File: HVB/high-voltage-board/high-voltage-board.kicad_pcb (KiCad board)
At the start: 2 copper layers, 181.6 x 106 mm, 73 parts, among them J1 Conn_01x23, J10 Conn_01x05, J11 HV-, J2 HECS, J3 HV+, J4 HV-, J5 HV+, J6 HV-, J7 Conn_01x02, J8 HV+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

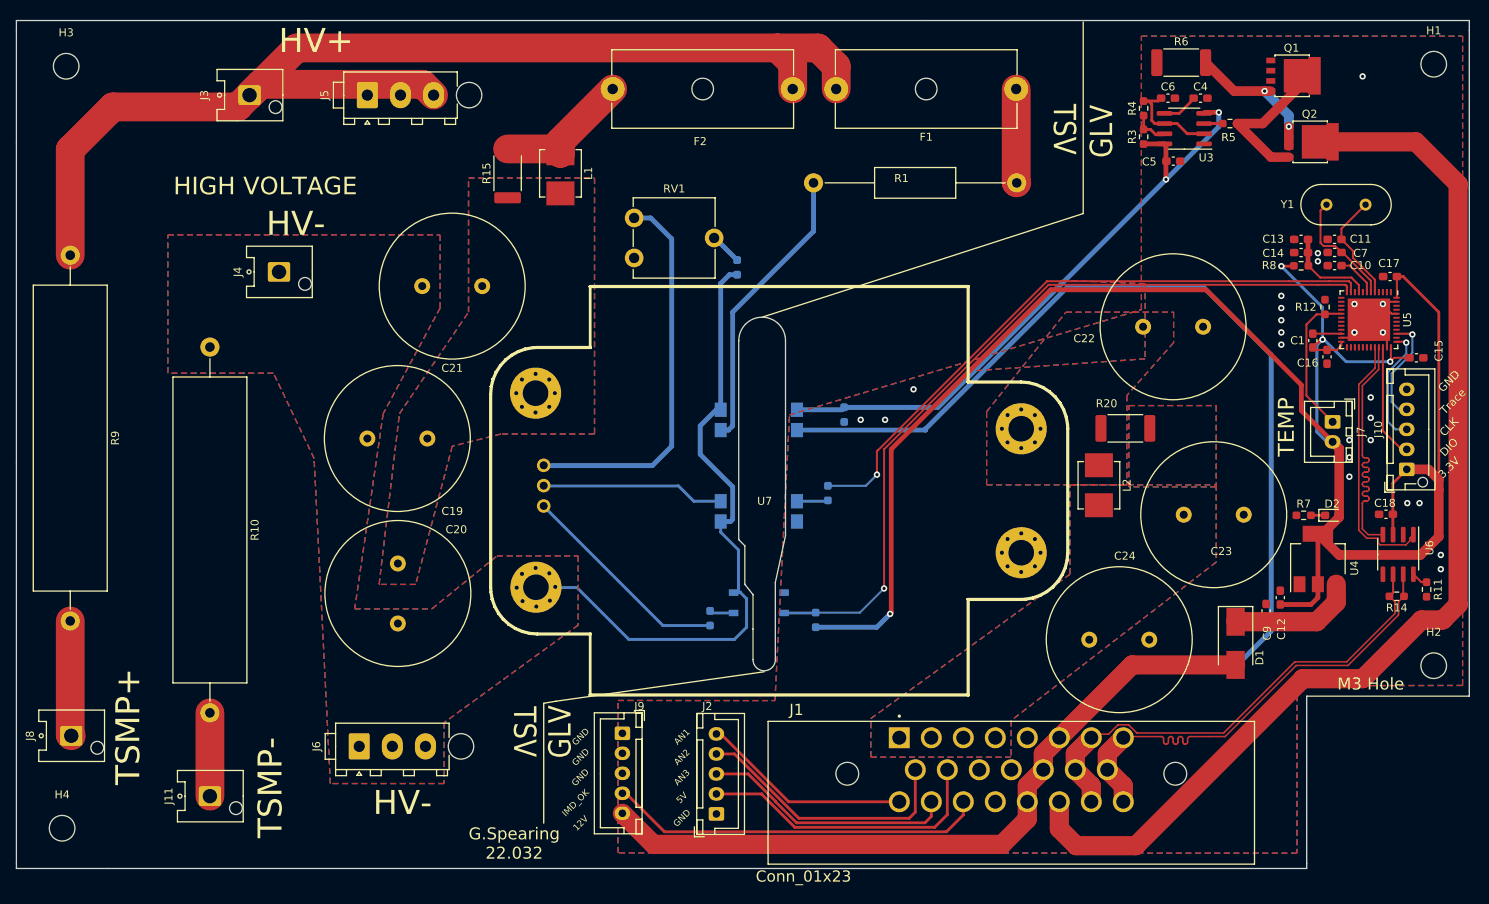
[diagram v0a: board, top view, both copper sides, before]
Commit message: Major Review and Part Update
updating footprints, component values, layouts
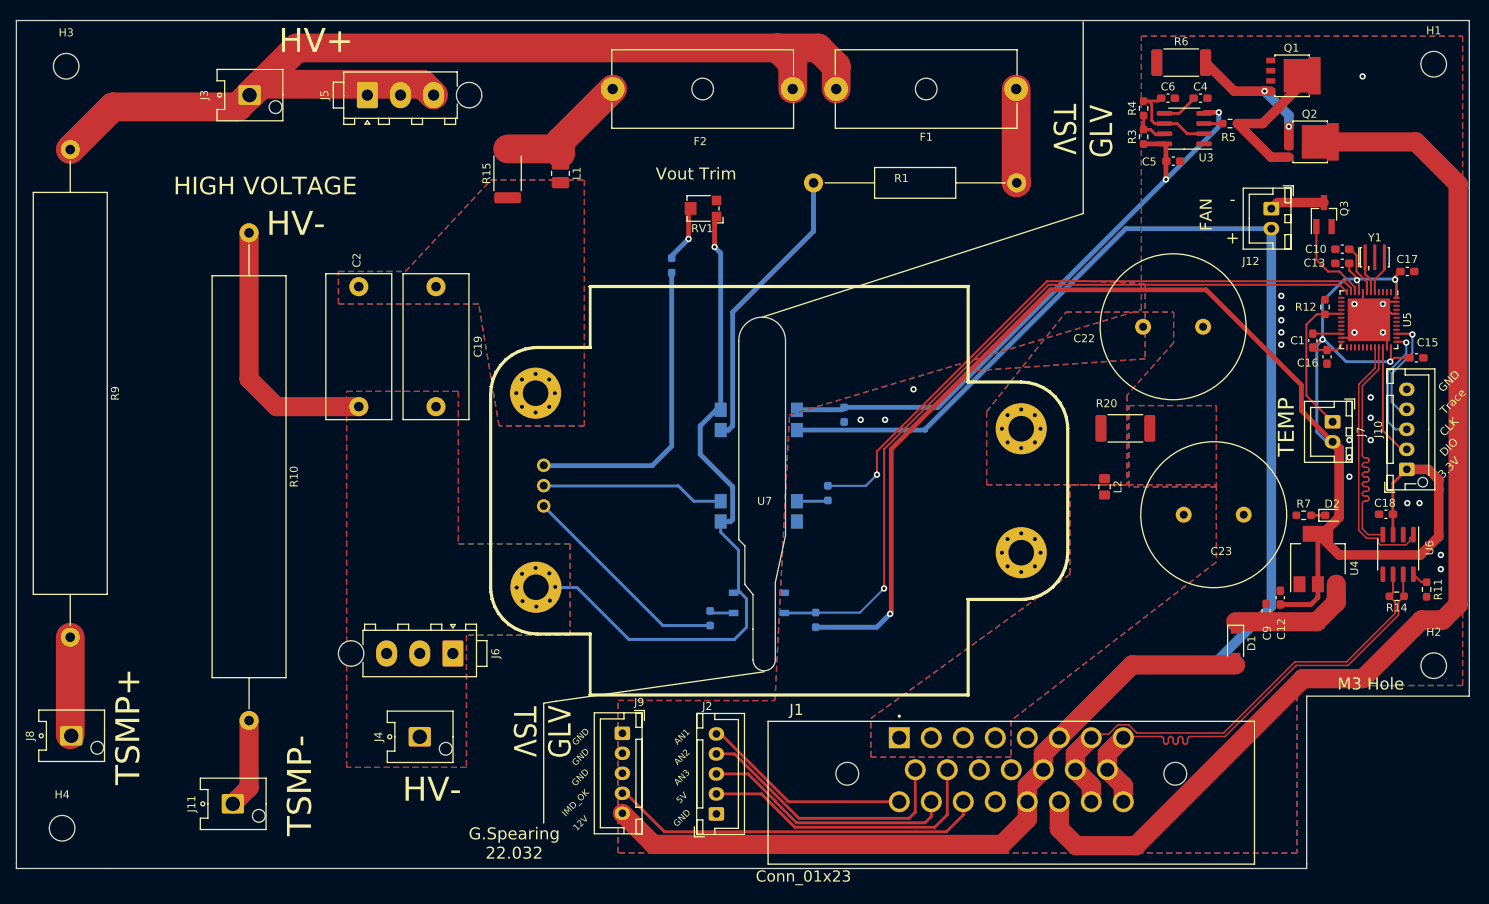
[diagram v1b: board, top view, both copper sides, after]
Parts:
- removed C11, C7: 20p, Capacitor_SMD:C_0603_1608Metric_Pad1.08x0.95mm_HandSolder
- removed C14: 0.1u, Capacitor_SMD:C_0603_1608Metric_Pad1.08x0.95mm_HandSolder
- removed C20, C21: 0.68uF, Capacitor_THT:C_Radial_D18.0mm_H35.5mm_P7.50mm
- removed C24: 4700uF, Capacitor_THT:C_Radial_D18.0mm_H35.5mm_P7.50mm
- removed R16: 6.8k, Resistor_SMD:R_0603_1608Metric_Pad0.98x0.95mm_HandSolder
- added C2: 0.68uF, Capacitor_THT:C_Rect_L18.0mm_W8.0mm_P15.00mm_FKS3_FKP3, F.Cu at (90.4, 72.0)
- added J12: Conn_01x02, Connector_JST:JST_XH_B2B-XH-A_1x02_P2.50mm_Vertical, F.Cu at (204.5, 62.2)
- added Q3: DMN3404L, Package_TO_SOT_SMD:SOT-23_Handsoldering, F.Cu at (211.1, 63.0)
- C19: footprint Capacitor_THT:C_Radial_D18.0mm_H35.5mm_P7.50mm -> Capacitor_THT:C_Rect_L18.0mm_W8.0mm_P15.00mm_FKS3_FKP3
- D1: value D_Schottky -> BAT54GW; footprint Diode_SMD:D_SMB_Handsoldering -> Diode_SMD:D_SOD-123
- F2: value 2A -> 35A
- L1: footprint Inductor_SMD:L_Murata_LQH55DN_5.7x5.0mm -> Inductor_SMD:L_1008_2520Metric_Pad1.43x2.20mm_HandSolder
- L2: footprint Inductor_SMD:L_Murata_LQH55DN_5.7x5.0mm -> Inductor_SMD:L_0805_2012Metric_Pad1.15x1.40mm_HandSolder
- R10, R9: value R -> 10k; footprint Resistor_THT:R_Axial_Power_L38.0mm_W9.0mm_P45.72mm -> Resistor_THT:R_Axial_Power_L50.0mm_W9.0mm_P60.96mm
- R15, R20: value 1Ω -> 1
- R7: value 220 -> 330
- R8: value R -> 300; moved to B.Cu
- RV1: value 50k -> 50k TC33x-2-503E; footprint Potentiometer_THT:Potentiometer_ACP_CA9-V10_Vertical -> Potentiometer_SMD:Potentiometer_Bourns_TC33X_Vertical
- Y1: value Crystal -> CSTME8M00; footprint Crystal:Crystal_HC49-U_Vertical -> AERO_Footprints:Resonator_SMD_muRata_CSTxExxV-3Pin_3.0x1.1mm_HandSoldering
- moved R8 78.7 mm to (129.5, 69.3), turned to 90 degrees
- moved J4 60.7 mm to (98.0, 128.3)
- moved C19 19.0 mm to (100.1, 72.0), turned to -90 degrees
- moved J6 16.5 mm to (102.2, 117.9), turned to -90 degrees
- moved R10 15.1 mm to (76.7, 65.3)
- moved R9 13.2 mm to (54.4, 54.9)
- moved RV1 10.5 mm to (133.3, 62.2), turned to 180 degrees
- moved Y1 8.92 mm to (217.4, 68.3)
- moved C13 5.95 mm to (213.4, 69.1)
- moved J11 3.02 mm to (74.7, 136.7)
- moved C10 2.27 mm to (213.4, 67.3)
- moved C17 2.25 mm to (221.5, 70.1), turned to 0 degrees
- moved L2 0.73 mm to (183.6, 97.0)
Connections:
- C13 pad 2: Net-(C13-Pad2) -> +3V3
- R8 pad 1: Net-(C13-Pad2) -> /vicor/TRIM_HV
- R8 pad 2: +3V3 -> Net-(RV1-Pad2)
- RV1 pad 1: unconnected-(RV1-Pad1) -> HV-
- RV1 pad 2: Net-(R16-Pad1) -> Net-(RV1-Pad2)
- RV1 pad 3: /DC_DC_TRIM_EN -> unconnected-(RV1-Pad3)
- U5 pad 10: unconnected-(U5-Pad10) -> /controller/FAN_SIG
- U5 pad 5: Net-(C11-Pad2) -> Net-(U5-Pad5)
- U5 pad 8: unconnected-(U5-Pad8) -> GND
- U5 pad 9: Net-(C13-Pad2) -> +3V3
- U7 pad 2: /DC_DC_TRIM_EN -> /vicor/TRIM_HV
- Y1 pad 2: Net-(C11-Pad2) -> GND
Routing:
- net /DC_DC_TRIM_EN: track 48.7 -> 0.00 mm
- net HV-: track 81.7 -> 121.5 mm, vias 0 -> 1
- net /vicor/TRIM_HV: track 0.00 -> 38.7 mm
- net +3V3: track 247.5 -> 225.5 mm, vias 4 -> 5
- net Net-(C11-Pad2): track 13.9 -> 0.00 mm
- net +12V: track 228.0 -> 241.5 mm
- net HV+: track 148.1 -> 134.9 mm
- net Net-(C13-Pad2): track 11.5 -> 0.00 mm
- net /controller/FAN_SIG: track 0.00 -> 11.0 mm
- net Net-(U5-Pad6): track 14.8 -> 4.66 mm
- net Net-(J12-Pad1): track 0.00 -> 6.90 mm
- net Net-(RV1-Pad2): track 0.00 -> 6.89 mm, vias 0 -> 1
- net Net-(U5-Pad5): track 0.00 -> 4.86 mm
- net Net-(R16-Pad1): track 4.02 -> 0.00 mm
- net GND: track 7.84 -> 11.6 mm, vias 25 -> 23
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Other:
- board text added: "- +"
- board text added: "FAN"
- board text added: "Vout Trim"

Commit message: updating layout and minor schem updates
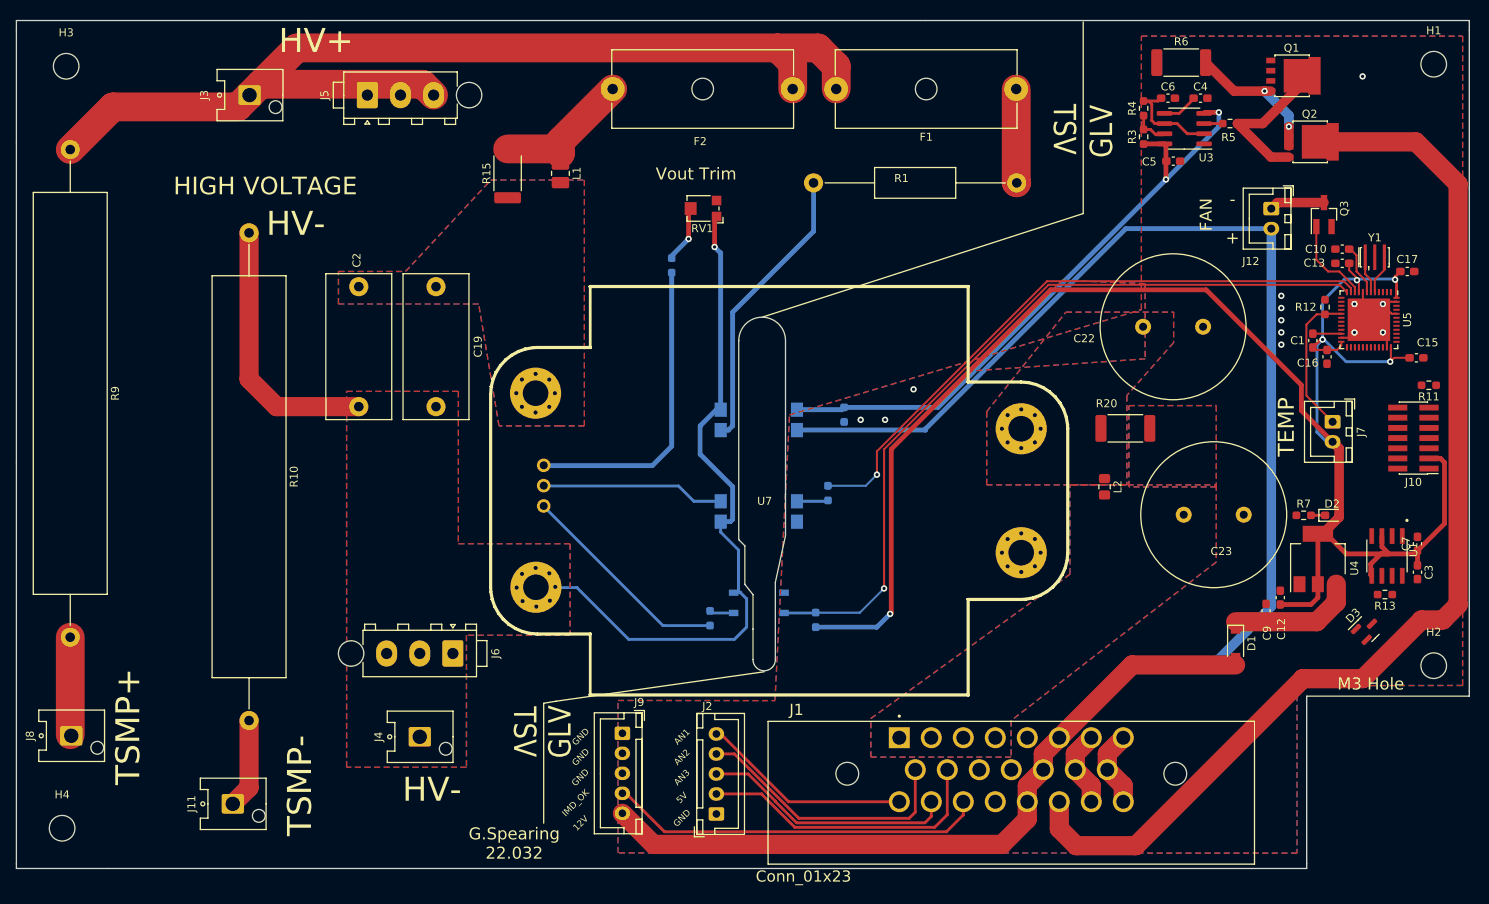
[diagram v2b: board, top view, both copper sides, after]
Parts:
- removed C18: 0.1u, Capacitor_SMD:C_0603_1608Metric_Pad1.08x0.95mm_HandSolder
- removed R14: 120, Resistor_SMD:R_0603_1608Metric_Pad0.98x0.95mm_HandSolder
- removed U6: MCP2551-I-SN, Package_SO:SOIC-8_3.9x4.9mm_P1.27mm
- added C3: 0.1u, Capacitor_SMD:C_0603_1608Metric_Pad1.08x0.95mm_HandSolder, F.Cu at (222.8, 107.7)
- added C7: 0.1u, Capacitor_SMD:C_0603_1608Metric_Pad1.08x0.95mm_HandSolder, F.Cu at (222.8, 104.1)
- added D3: SP0502BAHT, Package_TO_SOT_SMD:SOT-23, F.Cu at (216.4, 114.8)
- added R13: 120, Resistor_SMD:R_0603_1608Metric_Pad0.98x0.95mm_HandSolder, F.Cu at (218.7, 110.5)
- added U1: MAX33054EASA+T, AERO_Footprints:SOIC127P600X175-8N, F.Cu at (218.9, 105.7)
- J10: value Conn_01x05 -> FTSH-107-01-F-DV-k; footprint Connector_JST:JST_XH_B5B-XH-AM_1x05_P2.50mm_Vertical -> Connector_PinHeader_1.27mm:PinHeader_2x07_P1.27mm_Vertical_SMD
- R11: value 1k -> 100
- moved R11 25.5 mm to (224.2, 84.3), turned to 180 degrees
- moved J10 4.00 mm to (222.2, 90.9), turned to 180 degrees
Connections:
- J10 pad 1: +3V3 -> unconnected-(J10-Pad1)
- J10 pad 2: A13_SWDIO -> unconnected-(J10-Pad2)
- J10 pad 3: A14_SWCLK -> +3V3
- J10 pad 4: B3_TRACESWO -> A13_SWDIO
- R11 pad 1: Net-(R11-Pad1) -> GND
- R11 pad 2: GND -> Net-(J10-Pad11)
- U5 pad 32: /controller/CAN_X_P -> /controller/CAN_RX
- U5 pad 33: /controller/CAN_X_N -> /controller/CAN_TX
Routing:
- net /CAN-: track 60.3 -> 9.66 mm
- net /CAN+: track 59.9 -> 9.66 mm
- net /controller/CAN_X_P: track 32.4 -> 0.00 mm
- net /controller/CAN_X_N: track 32.1 -> 0.00 mm
- net A14_SWCLK: track 14.9 -> 0.00 mm, vias 1 -> 0
- net A13_SWDIO: track 14.4 -> 0.00 mm
- net B3_TRACESWO: track 13.8 -> 0.00 mm, vias 1 -> 0
- net GND: track 11.6 -> 7.36 mm, vias 23 -> 13
- net +3V3: track 225.5 -> 222.1 mm
- net Net-(R11-Pad1): track 2.06 -> 0.00 mm
- net HV+: track 134.9 -> 132.9 mm
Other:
- board text removed: "3.3V"
- board text removed: "CLK"
- board text removed: "DIO"
- board text removed: "Trace"

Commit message: finish layout ready for review
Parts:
- added JP1: SolderJumper_2_Bridged, Jumper:SolderJumper-2_P1.3mm_Bridged_RoundedPad1.0x1.5mm, F.Cu at (223.3, 75.6)
- C13, C15, C16, C17: moved to B.Cu
- moved C17 4.33 mm to (222.5, 74.3), turned to -90 degrees
- moved C15 4.09 mm to (218.6, 81.5), turned to 180 degrees
- moved C16 2.77 mm to (214.1, 81.5), turned to 0 degrees
- moved C13 0.11 mm to (213.3, 69.0)
- turned C10 to 0 degrees
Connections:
- C10 pad 1: Net-(C10-Pad1) -> GND
- C10 pad 2: GND -> Net-(U5-Pad7)
- D3 pad 1: /controller/CAN_N -> /CAN-
- D3 pad 2: /controller/CAN_P -> /CAN+
- D3 pad 3: unconnected-(D3-Pad3) -> GND
- R13 pad 1: /controller/CAN_P -> /CAN+
- R13 pad 2: /controller/CAN_N -> /CAN-
- U1 pad 1: unconnected-(U1-Pad1) -> /controller/CAN_TX
- U1 pad 6: /controller/CAN_N -> /CAN-
- U1 pad 7: /controller/CAN_P -> /CAN+
- U5 pad 44: GND -> Net-(U5-Pad44)
- U5 pad 7: Net-(C10-Pad1) -> Net-(U5-Pad7)
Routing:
- net /CAN-: track 9.66 -> 59.5 mm
- net /CAN+: track 9.66 -> 59.4 mm
- net /controller/CAN_TX: track 0.00 -> 25.6 mm
- net /controller/CAN_RX: track 0.00 -> 25.6 mm
- net A14_SWCLK: track 0.00 -> 17.6 mm
- net B3_TRACESWO: track 0.00 -> 17.3 mm
- net A13_SWDIO: track 0.00 -> 16.5 mm
- net +3V3: track 222.1 -> 235.3 mm
- net Net-(U5-Pad7): track 0.00 -> 6.23 mm
- net Net-(C10-Pad1): track 6.23 -> 0.00 mm
- net Net-(J10-Pad11): track 0.00 -> 5.73 mm
- net Net-(U5-Pad44): track 0.00 -> 2.56 mm
- net GND: track 7.36 -> 6.12 mm, vias 13 -> 18

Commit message: touching up layout and making gerbers
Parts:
- removed D1: BAT54GW, Diode_SMD:D_SOD-123
- moved R7 3.68 mm to (212.2, 100.6)
- moved D2 3.44 mm to (208.6, 100.6)
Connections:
- C9 pad 1: Net-(C9-Pad1) -> +12V
- D2 pad 1: Net-(D2-Pad1) -> GND
- D2 pad 2: +3V3 -> Net-(D2-Pad2)
- R7 pad 1: GND -> Net-(D2-Pad2)
- R7 pad 2: Net-(D2-Pad1) -> +3V3
- U4 pad 3: Net-(C9-Pad1) -> +12V
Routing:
- net +12V: track 241.5 -> 259.3 mm
- net Net-(C9-Pad1): track 15.8 -> 0.00 mm
- net Net-(D2-Pad2): track 0.00 -> 1.78 mm
- net Net-(D2-Pad1): track 1.77 -> 0.00 mm
- net Net-(J10-Pad11): track 5.73 -> 4.70 mm
- net +3V3: track 235.3 -> 234.4 mm
- net B3_TRACESWO: track 17.3 -> 16.4 mm
- net /CAN-: track 59.5 -> 58.9 mm
- net GND: vias 18 -> 16
